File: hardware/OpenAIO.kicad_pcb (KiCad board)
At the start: 8 copper layers, 35 x 35 mm, 341 parts, among them J15 5V, J16 5V, J17 5V, J18 5V, J20 5V, J21 5V, J23 5V, J24 5V, J25 5V, J26 5V, J27 5V, J28 5V, J29 5V, J30 5V, J31 5V, J32 5V, J33 5V, J34 5V, J35 5V, J37 5V, J38 5V, J39 5V, J40 5V, J41 5V, J42 5V, J43 5V, J44 5V, J45 5V, J48 5V, J49 5V, J50 5V, J51 5V, J52 5V, J53 5V, J54 5V, J55 5V, Q1 AP1606, Q10 DOY180N03T, Q11 DOY180N03T, Q12 DOY180N03T, Q13 DOY180N03T, Q14 DOY180N03T, Q15 DOY180N03T, Q16 DOY180N03T, Q17 DOY180N03T, Q18 DOY180N03T, Q19 DOY180N03T, Q2 AP1606, Q20 DOY180N03T, Q21 DOY180N03T, Q22 DOY180N03T, Q23 DOY180N03T, Q24 DOY180N03T, Q25 DOY180N03T, Q26 DOY180N03T, Q3 DOY180N03T, Q4 DOY180N03T, Q5 DOY180N03T, Q6 DOY180N03T, Q7 DOY180N03T, Q8 DOY180N03T, Q9 DOY180N03T, U1 TS2306A 240GF MSM 9_C2976675, U10 COS8051SOT, U11 TLV7031DPWR, U12 SM06B-SRSS-TB(LF)(SN), U13 AT32F421G8U7, U14 NSG2065Q, U15 AT32F421G8U7, U16 NSG2065Q, U17 AT32F421G8U7, U18 NSG2065Q, U19 AT32F421G8U7, U2 RP2354A, U20 NSG2065Q, U21 SX1281IMLTRT, U22 ESP32-C3, U24 AIO_outline, U25 INA186A3IDCKR, U26 BMP580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

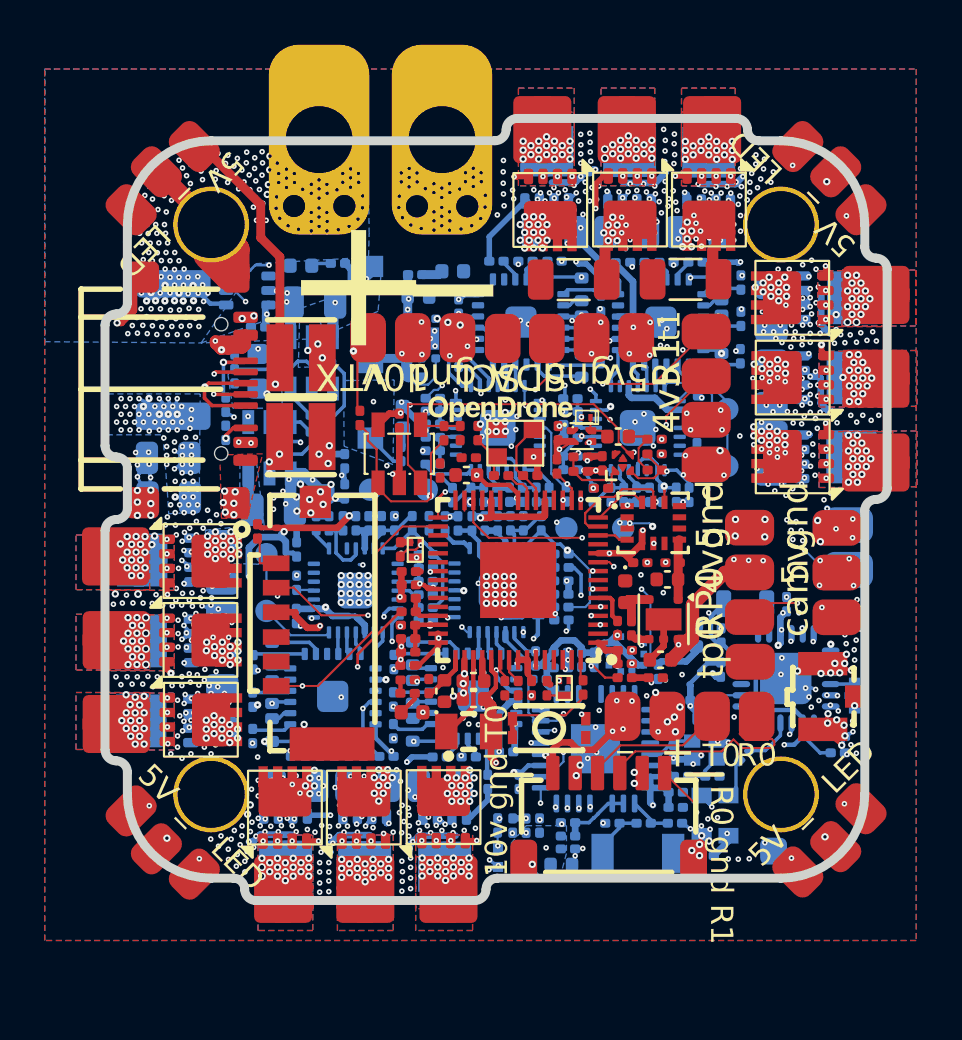
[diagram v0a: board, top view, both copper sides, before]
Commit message: Edit form again: one via per connection, no stacks
tools/via_collapse.py: each non-GND microvia + buried stack becomes one
0.33/0.15 via over the layers it spanned (blind L1-L7 / L2-L8, buried L2-L7,
through where L1 and L8 meet). Vias that would short or crowd a neighbour
once longer are turned back (--keep). GND keeps its plane microvias.

| | Before | After |
|---|---|---|
| Non-GND stacks | 533 | 1 (+3.3V, would clip /4A on L3) |
| DRC errors | 2 (/3A via forms) | 0 |
| Unconnected | 78 | 78 (no net worse) |

Also: 2 blind L3-L8 vias (/3A, /4A) to L2-L8; a /3A L7-L8 microvia that sat
inside a blind L3-L8 removed. via_types.py rebuilds the stacks at the end.

Co-Authored-By: Claude Opus 5.5 <noreply@anthropic.com>
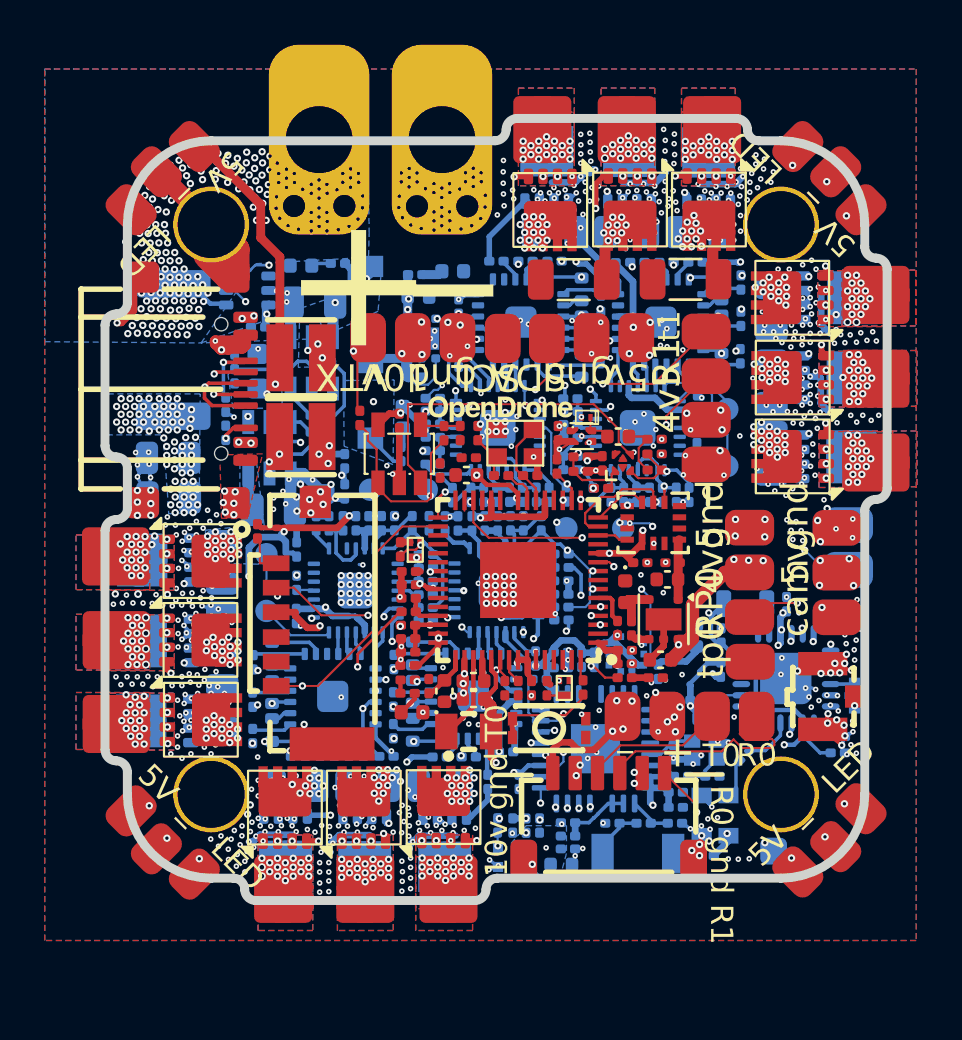
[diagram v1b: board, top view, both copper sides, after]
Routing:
- net USB_D-: vias 5 -> 3
- net USB_D+: vias 3 -> 2
- net UART1_TX: vias 4 -> 2
- net UART1_RX: vias 6 -> 3
- net SPI0.MOSI: vias 4 -> 2
- net Net-(U3-FB): vias 4 -> 2
- net Net-(U21-DCC_FB): vias 5 -> 3
- net Net-(U17-PA14): vias 6 -> 3
- net Net-(U17-PA13): vias 4 -> 2
- net Net-(U15-PA14): vias 4 -> 2
- net Net-(U15-PA13): vias 4 -> 2
- net Net-(U13-PA14): vias 4 -> 2
- net Net-(Q9-G): vias 4 -> 2
- net Net-(Q8-G): vias 2 -> 1
- net Net-(Q7-G): vias 4 -> 2
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
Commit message: IO remap: shortest RP2354A runs on the placed board; SBUS back on UART0
tools/io_opt.py (constraint-checked assignment, research/IO-CONSTRAINTS.md)
picked the mapping; tools/io_remap_sch.py edits the sheets (sexpdata),
re-saved with kicad-cli; netlist diff shows only the intended pins changed.

| Net | GPIO before | GPIO after |
|---|---|---|
| MOTOR2 | 24 | 21 |
| MOTOR3 | 23 | 18 |
| MOTOR4 | 22 | 8 |
| SPI0.SCK (SD) | 18 | 22 |
| FLASH_CS (SD CS) | 21 | 24 |
| LED_STRIP_L | 8 | 26 |
| LED0 | 26 | 27 |
| free | 27 | 23 |

U2-to-part distance 147.2 -> 136.5 mm; UART, I2C, SPI1, OSD, ADC unchanged.
SH-6 pin 6 (air unit SBUS) moved from UART1_RX, where it fought the ESP32
TX, to PU0RX (hardware UART0 RX, GPIO3) as config.h intends.
Board: pad nets synced, 2.3 mm UART1_RX stub at U12.6 removed.
DRC 0 errors, unconnected 78 -> 79 (U12.6 to PU0RX to route).
config.h and PINOUT.md updated.

Co-Authored-By: Claude Opus 5.5 <noreply@anthropic.com>
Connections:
- U12 pad 6: UART1_RX -> /Pads/PU0RX
- U2 pad 12: /RP2354A/LED_STRIP_L -> MOTOR4
- U2 pad 29: SPI0.SCK -> MOTOR3
- U2 pad 33: FLASH_CS -> MOTOR2
- U2 pad 34: MOTOR4 -> SPI0.SCK
- U2 pad 35: MOTOR3 -> unconnected-(U2-GPIO23-Pad35)
- U2 pad 36: MOTOR2 -> FLASH_CS
- U2 pad 40: /RP2354A/LED0 -> /RP2354A/LED_STRIP_L
- U2 pad 41: unconnected-(U2-GPIO27_ADC1-Pad41) -> /RP2354A/LED0
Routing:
- net UART1_RX: track 26.6 -> 24.3 mm
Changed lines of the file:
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@@
 			(size 0.875 0.2)
 			(layers "F.Cu" "F.Mask" "F.Paste")
-			(net "/RP2354A/LED_STRIP_L")
+			(net "MOTOR4")
 			(pinfunction "GPIO8_12")
 			(pintype "unspecified")
@@
 			(size 0.2 0.875)
 			(layers "F.Cu" "F.Mask" "F.Paste")
-			(net "SPI0.SCK")
+			(net "MOTOR3")
 			(pinfunction "GPIO18_29")
 			(pintype "unspecified")
@@
 			(size 0.875 0.2)
 			(layers "F.Cu" "F.Mask" "F.Paste")
-			(net "FLASH_CS")
+			(net "MOTOR2")
 			(pinfunction "GPIO21_33")
 			(pintype "unspecified")
@@
 			(size 0.875 0.2)
 			(layers "F.Cu" "F.Mask" "F.Paste")
-			(net "MOTOR4")
+			(net "SPI0.SCK")
 			(pinfunction "GPIO22_34")
 			(pintype "unspecified")
@@
 			(size 0.875 0.2)
 			(layers "F.Cu" "F.Mask" "F.Paste")
-			(net "MOTOR3")
+			(net "unconnected-(U2-GPIO23-Pad35)")
 			(pinfunction "GPIO23_35")
-			(pintype "unspecified")
+			(pintype "unspecified+no_connect")
 		)
 		(pad "36" smd rect
@@
 			(size 0.875 0.2)
 			(layers "F.Cu" "F.Mask" "F.Paste")
-			(net "MOTOR2")
+			(net "FLASH_CS")
 			(pinfunction "GPIO24_36")
 			(pintype "unspecified")
@@
 			(size 0.875 0.2)
 			(layers "F.Cu" "F.Mask" "F.Paste")
-			(net "/RP2354A/LED0")
+			(net "/RP2354A/LED_STRIP_L")
 			(pinfunction "GPIO26_ADC0_40")
 			(pintype "unspecified")
@@
 			(size 0.875 0.2)
 			(layers "F.Cu" "F.Mask" "F.Paste")
-			(net "unconnected-(U2-GPIO27_ADC1-Pad41)")
+			(net "/RP2354A/LED0")
 			(pinfunction "GPIO27_ADC1_41")
-			(pintype "unspecified+no_connect")
+			(pintype "unspecified")
 		)
 		(pad "42" smd rect
@@
 			(layers "F.Cu" "F.Mask" "F.Paste")
 			(roundrect_rratio 0.15)
-			(net "UART1_RX")
+			(net "/Pads/PU0RX")
 			(pinfunction "6_6")
 			(pintype "unspecified")
@@
 	)
 	(segment
-		(start 82.94 72.7075)
-		(end 84.3742 74.1417)
-		(width 0.09)
-		(layer "F.Cu")
-		(net "UART1_RX")
-	)
-	(segment
 		(start 80.4733 63.27)
 		(end 80.6701 63.4668)
@@
 	)
 	(segment
-		(start 84.3742 74.1417)
-		(end 84.3742 74.4613)
-		(width 0.09)
-		(layer "F.Cu")
-		(net "UART1_RX")
-	)
-	(segment
 		(start 80.28 63.27)
 		(end 80.4733 63.27)
@@
 	)
 	(segment
-		(start 78.673854 68.555)
-		(end 78.673854 68.456504)
+		(start 79.965104 62.47)
+		(end 79.67 62.47)
 		(width 0.1)
 		(layer "F.Cu")
-		(net "/RP2354A/LED_STRIP_L")
+		(net "MOTOR4")
 	)
 	(segment
-		(start 79.965104 62.47)
-		(end 79.67 62.47)
+		(start 84.22 58.17)
+		(end 84.22 58.94)
 		(width 0.1)
-		(layer "F.Cu")
-		(net "/RP2354A/LED_STRIP_L")
+		(layer "B.Cu")
+		(net "MOTOR4")
 	)
 	(segment
-		(start 78.673854 68.456504)
-		(end 78.675831 68.454527)
+		(start 84.390064 57.999936)
+		(end 84.22 58.17)
 		(width 0.1)
-		(layer "F.Cu")
-		(net "/RP2354A/LED_STRIP_L")
+		(layer "B.Cu")
+		(net "MOTOR4")
+	)
+	(segment
+		(start 84.390064 57.930944)
+		(end 84.390064 57.999936)
+		(width 0.1)
+		(layer "B.Cu")
+		(net "MOTOR4")
+	)
+	(segment
+		(start 84.22 58.94)
+		(end 84.13 59.03)
+		(width 0.1)
+		(layer "B.Cu")
+		(net "MOTOR4")
+	)
+	(via blind
+		(at 84.13 59.03)
+		(size 0.33)
+		(drill 0.15)
+		(layers "In1.Cu" "B.Cu")
+		(net "MOTOR4")
 	)
 	(segment
@@
 		(width 0.1)
 		(layer "F.Cu")
-		(net "SPI0.SCK")
+		(net "MOTOR3")
+	)
+	(segment
+		(start 78.536875 60.558113)
+		(end 78.491887 60.558113)
+		(width 0.1)
+		(layer "B.Cu")
+		(net "MOTOR3")
+	)
+	(segment
+		(start 78.491887 60.558113)
+		(end 78.49 60.56)
+		(width 0.1)
+		(layer "B.Cu")
+		(net "MOTOR3")
 	)
 	(segment
@@
 	)
 	(segment
+		(start 72.4 61.2)
+		(end 72.36 61.16)
+		(width 0.1)
+		(layer "B.Cu")
+		(net "MOTOR2")
+	)
+	(segment
+		(start 72.4 61.205)
+		(end 72.4 61.2)
+		(width 0.1)
+		(layer "B.Cu")
+		(net "MOTOR2")
+	)
+	(segment
 		(start 64.8233 62.3133)
 		(end 64.8233 63.3175)
@@
 	)
 	(segment
-		(start 84.22 58.17)
-		(end 84.22 58.94)
-		(width 0.1)
-		(layer "B.Cu")
-		(net "MOTOR4")
-	)
-	(segment
-		(start 84.390064 57.999936)
-		(end 84.22 58.17)
-		(width 0.1)
-		(layer "B.Cu")
-		(net "MOTOR4")
-	)
-	(segment
-		(start 84.390064 57.930944)
-		(end 84.390064 57.999936)
-		(width 0.1)
-		(layer "B.Cu")
-		(net "MOTOR4")
-	)
-	(segment
-		(start 84.22 58.94)
-		(end 84.13 59.03)
-		(width 0.1)
-		(layer "B.Cu")
-		(net "MOTOR4")
-	)
-	(via blind
-		(at 84.13 59.03)
-		(size 0.33)
-		(drill 0.15)
-		(layers "In1.Cu" "B.Cu")
-		(net "MOTOR4")
-	)
-	(segment
-		(start 78.536875 60.558113)
-		(end 78.491887 60.558113)
-		(width 0.1)
-		(layer "B.Cu")
-		(net "MOTOR3")
-	)
-	(segment
-		(start 78.491887 60.558113)
-		(end 78.49 60.56)
-		(width 0.1)
-		(layer "B.Cu")
-		(net "MOTOR3")
-	)
-	(segment
-		(start 72.4 61.2)
-		(end 72.36 61.16)
-		(width 0.1)
-		(layer "B.Cu")
-		(net "MOTOR2")
-	)
-	(segment
-		(start 72.4 61.205)
-		(end 72.4 61.2)
-		(width 0.1)
-		(layer "B.Cu")
-		(net "MOTOR2")
-	)
-	(segment
 		(start 72.805104 63.67)
 		(end 72.456689 63.703272)
@@
 	)
 	(segment
+		(start 78.673854 68.555)
+		(end 78.673854 68.456504)
+		(width 0.1)
+		(layer "F.Cu")
+		(net "/RP2354A/LED_STRIP_L")
+	)
+	(segment
+		(start 78.673854 68.456504)
+		(end 78.675831 68.454527)
+		(width 0.1)
+		(layer "F.Cu")
+		(net "/RP2354A/LED_STRIP_L")
+	)
+	(segment
